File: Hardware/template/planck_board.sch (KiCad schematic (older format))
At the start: 3 parts, among them J1 Conn_01x40

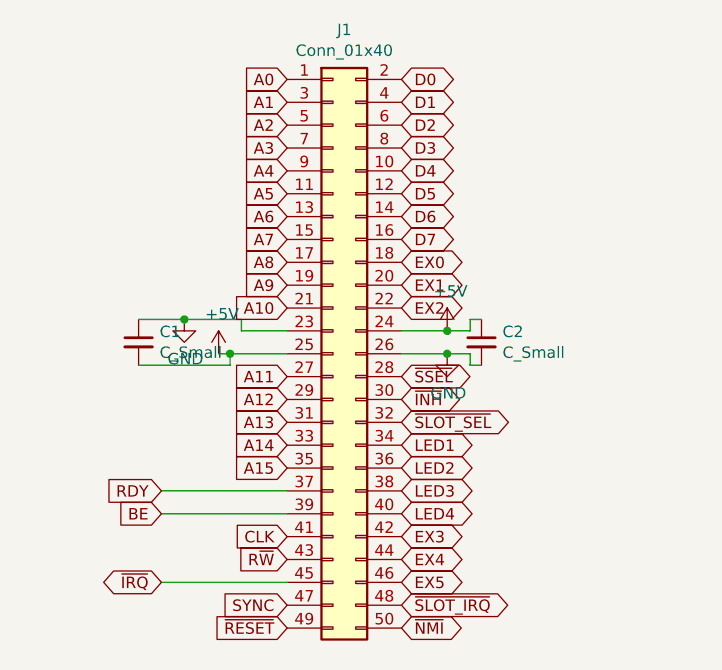
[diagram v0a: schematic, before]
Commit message: Space pins for better legibility
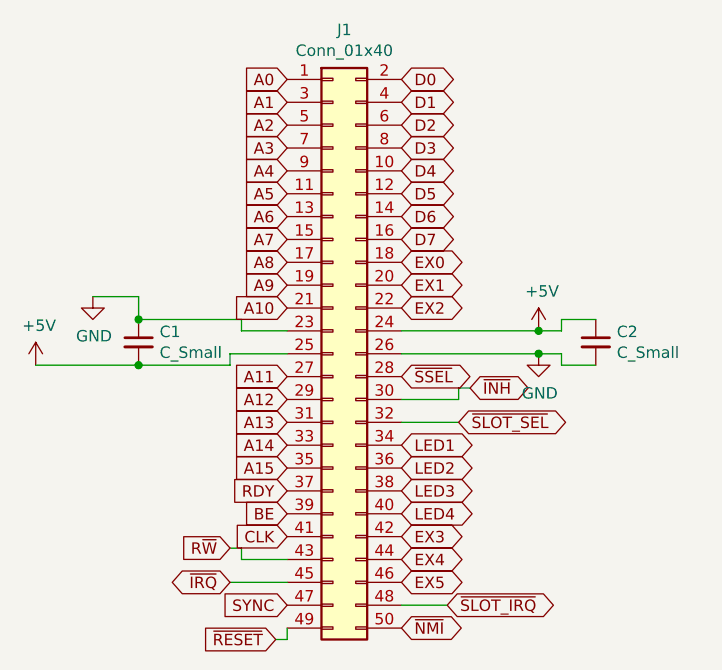
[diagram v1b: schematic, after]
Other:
- moved on the sheet: C2
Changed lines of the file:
@@
 L power:+5V #PWR0101
 U 1 1 5FD64472
-P 2650 3450
-F 0 "#PWR0101" H 2650 3300 50  0001 C CNN
-F 1 "+5V" H 2665 3623 50  0000 C CNN
-F 2 "" H 2650 3450 50  0001 C CNN
-F 3 "" H 2650 3450 50  0001 C CNN
-	1    2650 3450
-	1    0    0    -1
-$EndComp
-Wire Wire Line
-	2650 3450 2450 3450
+P 3050 3450
+F 0 "#PWR0101" H 3050 3300 50  0001 C CNN
+F 1 "+5V" H 3065 3623 50  0000 C CNN
+F 2 "" H 3050 3450 50  0001 C CNN
+F 3 "" H 3050 3450 50  0001 C CNN
+	1    3050 3450
+	1    0    0    -1
+$EndComp
 $Comp
 L power:+5V #PWR0102
 U 1 1 5FD65A34
-P 1650 3550
-F 0 "#PWR0102" H 1650 3400 50  0001 C CNN
-F 1 "+5V" H 1665 3723 50  0000 C CNN
-F 2 "" H 1650 3550 50  0001 C CNN
-F 3 "" H 1650 3550 50  0001 C CNN
-	1    1650 3550
+P 850 3600
+F 0 "#PWR0102" H 850 3450 50  0001 C CNN
+F 1 "+5V" H 865 3773 50  0000 C CNN
+F 2 "" H 850 3600 50  0001 C CNN
+F 3 "" H 850 3600 50  0001 C CNN
+	1    850  3600
 	1    0    0    -1
 $EndComp
@@
 L power:GND #PWR0103
 U 1 1 5FD65E00
-P 2650 3550
-F 0 "#PWR0103" H 2650 3300 50  0001 C CNN
-F 1 "GND" H 2655 3377 50  0000 C CNN
-F 2 "" H 2650 3550 50  0001 C CNN
-F 3 "" H 2650 3550 50  0001 C CNN
-	1    2650 3550
-	1    0    0    -1
-$EndComp
-Wire Wire Line
-	2650 3550 2450 3550
+P 3050 3550
+F 0 "#PWR0103" H 3050 3300 50  0001 C CNN
+F 1 "GND" H 3055 3377 50  0000 C CNN
+F 2 "" H 3050 3550 50  0001 C CNN
+F 3 "" H 3050 3550 50  0001 C CNN
+	1    3050 3550
+	1    0    0    -1
+$EndComp
 $Comp
 L power:GND #PWR0104
 U 1 1 5FD66D1A
-P 1500 3400
-F 0 "#PWR0104" H 1500 3150 50  0001 C CNN
-F 1 "GND" H 1505 3227 50  0000 C CNN
-F 2 "" H 1500 3400 50  0001 C CNN
-F 3 "" H 1500 3400 50  0001 C CNN
-	1    1500 3400
+P 1100 3300
+F 0 "#PWR0104" H 1100 3050 50  0001 C CNN
+F 1 "GND" H 1105 3127 50  0000 C CNN
+F 2 "" H 1100 3300 50  0001 C CNN
+F 3 "" H 1100 3300 50  0001 C CNN
+	1    1100 3300
 	1    0    0    -1
 $EndComp
 Wire Wire Line
 	1750 3450 1750 3400
-Wire Wire Line
-	1750 3400 1500 3400
 Wire Wire Line
 	1750 3450 1950 3450
@@
 Text GLabel 2450 3050 2    50   BiDi ~ 0
 D7
-Text GLabel 1950 4750 0    50   Input ~ 0
+Text GLabel 1900 4800 0    50   Input ~ 0
 ~RESET~
 Text GLabel 2450 4750 2    50   BiDi ~ 0
 ~NMI~
-Text GLabel 1400 4150 0    50   Input ~ 0
+Text GLabel 1950 4150 0    50   Input ~ 0
 RDY
-Text GLabel 1400 4250 0    50   Input ~ 0
+Text GLabel 1950 4250 0    50   Input ~ 0
 BE
 Text GLabel 1950 4350 0    50   Input ~ 0
 CLK
-Text GLabel 1950 4450 0    50   Input ~ 0
+Text GLabel 1700 4400 0    50   Input ~ 0
 R~W~
 Text GLabel 1950 4650 0    50   Input ~ 0
 SYNC
-Text GLabel 1400 4550 0    50   BiDi ~ 0
+Text GLabel 1700 4550 0    50   BiDi ~ 0
 ~IRQ~
-Text GLabel 2450 4650 2    50   BiDi ~ 0
+Text GLabel 2650 4650 2    50   BiDi ~ 0
 ~SLOT_IRQ~
 Text GLabel 2450 4550 2    50   BiDi ~ 0
@@
 L Device:C_Small C2
 U 1 1 5FD8A65F
-P 2800 3500
-F 0 "C2" H 2892 3546 50  0000 L CNN
-F 1 "C_Small" H 2892 3455 50  0000 L CNN
-F 2 "Capacitor_SMD:C_1206_3216Metric_Pad1.42x1.75mm_HandSolder" H 2800 3500 50  0001 C CNN
-F 3 "~" H 2800 3500 50  0001 C CNN
-	1    2800 3500
-	1    0    0    -1
-$EndComp
-Wire Wire Line
-	2800 3400 2750 3400
-Wire Wire Line
-	2750 3400 2750 3450
-Wire Wire Line
-	2750 3450 2650 3450
-Connection ~ 2650 3450
-Wire Wire Line
-	2800 3600 2750 3600
-Wire Wire Line
-	2750 3600 2750 3550
-Wire Wire Line
-	2750 3550 2650 3550
-Connection ~ 2650 3550
+P 3300 3500
+F 0 "C2" H 3392 3546 50  0000 L CNN
+F 1 "C_Small" H 3392 3455 50  0000 L CNN
+F 2 "Capacitor_SMD:C_1206_3216Metric_Pad1.42x1.75mm_HandSolder" H 3300 3500 50  0001 C CNN
+F 3 "~" H 3300 3500 50  0001 C CNN
+	1    3300 3500
+	1    0    0    -1
+$EndComp
+Wire Wire Line
+	3150 3400 3150 3450
+Wire Wire Line
+	3150 3600 3150 3550
+Wire Wire Line
+	3150 3550 3050 3550
 $Comp
 L Device:C_Small C1
@@
 $EndComp
 Wire Wire Line
-	1300 3400 1500 3400
-Connection ~ 1500 3400
-Wire Wire Line
 	1300 3600 1700 3600
 Wire Wire Line
 	1700 3600 1700 3550
-Connection ~ 1700 3550
-Wire Wire Line
-	1700 3550 1650 3550
-Wire Wire Line
-	1400 4550 1950 4550
-Wire Wire Line
-	1400 4150 1950 4150
-Wire Wire Line
-	1400 4250 1950 4250
+Wire Wire Line
+	1700 4550 1950 4550
 Text GLabel 2450 3650 2    50   BiDi ~ 0
 ~SSEL~
-Text GLabel 2450 3750 2    50   BiDi ~ 0
+Text GLabel 2750 3700 2    50   BiDi ~ 0
 ~INH~
-Text GLabel 2450 3850 2    50   BiDi ~ 0
+Text GLabel 2700 3850 2    50   BiDi ~ 0
 ~SLOT_SEL~
 Text GLabel 2450 3950 2    50   BiDi ~ 0
@@
 Text GLabel 2450 3350 2    50   BiDi ~ 0
 EX2
+Wire Wire Line
+	2450 3450 3050 3450
+Connection ~ 3050 3450
+Wire Wire Line
+	3050 3450 3150 3450
+Wire Wire Line
+	3150 3400 3300 3400
+Wire Wire Line
+	2450 3550 3050 3550
+Connection ~ 3050 3550
+Wire Wire Line
+	3150 3600 3300 3600
+Wire Wire Line
+	2750 3700 2700 3700
+Wire Wire Line
+	2700 3700 2700 3750
+Wire Wire Line
+	2700 3750 2450 3750
+Wire Wire Line
+	2650 4650 2450 4650
+Wire Wire Line
+	1900 4800 1950 4800
+Wire Wire Line
+	1950 4800 1950 4750
+Wire Wire Line
+	1700 4400 1750 4400
+Wire Wire Line
+	1750 4400 1750 4450
+Wire Wire Line
+	1750 4450 1950 4450
+Wire Wire Line
+	2700 3850 2450 3850
+Wire Wire Line
+	1300 3400 1750 3400
+Wire Wire Line
+	1300 3400 1300 3300
+Wire Wire Line
+	1300 3300 1100 3300
+Connection ~ 1300 3400
+Wire Wire Line
+	1300 3600 850  3600
+Connection ~ 1300 3600
 $EndSCHEMATC

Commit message: Add clock stretching with counter and slow clock request from peripherals.
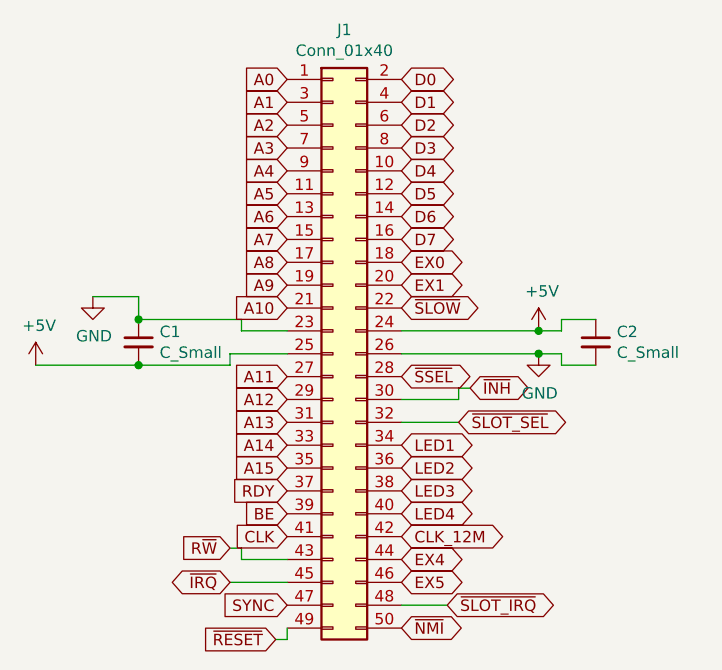
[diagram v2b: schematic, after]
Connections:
- net EX2 renamed ~SLOW~
- net EX3 renamed CLK_12M
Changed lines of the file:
@@
 EX4
 Text GLabel 2450 4350 2    50   BiDi ~ 0
-EX3
+CLK_12M
 $Comp
 L Device:C_Small C2
@@
 EX1
 Text GLabel 2450 3350 2    50   BiDi ~ 0
-EX2
+~SLOW~
 Wire Wire Line
 	2450 3450 3050 3450

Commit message: Many updates. SLOW signal is now shared amongst all slots, so their output has to be open drain.
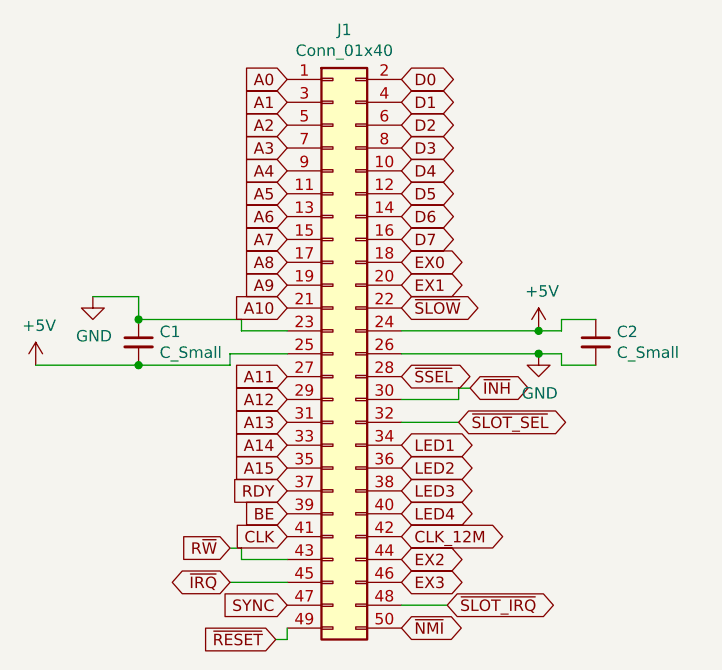
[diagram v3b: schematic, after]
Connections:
- net EX4 renamed EX2
- net EX5 renamed EX3
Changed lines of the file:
@@
 ~SLOT_IRQ~
 Text GLabel 2450 4550 2    50   BiDi ~ 0
-EX5
+EX3
 Text GLabel 2450 4450 2    50   BiDi ~ 0
-EX4
+EX2
 Text GLabel 2450 4350 2    50   BiDi ~ 0
 CLK_12M

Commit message: update pin names
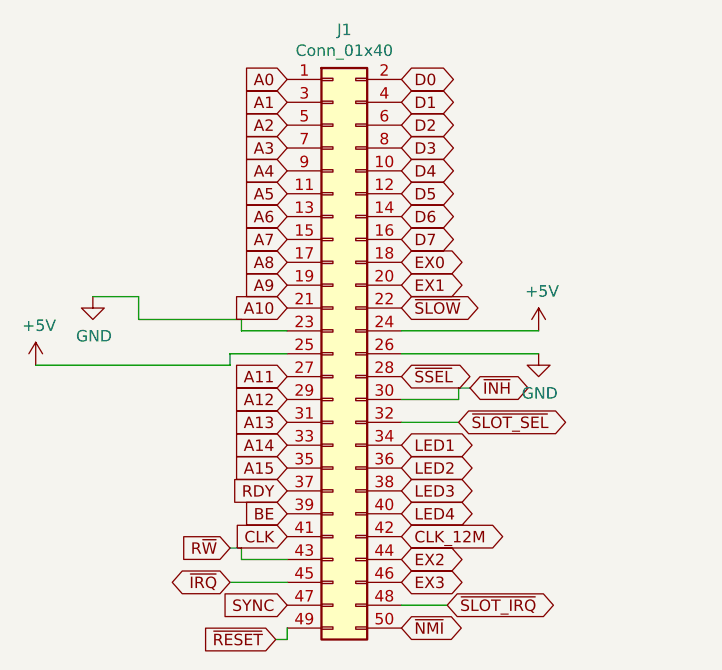
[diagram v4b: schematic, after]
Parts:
- removed C1, C2: C_Small, Capacitor_SMD:C_1206_3216Metric_Pad1.42x1.75mm_HandSolder, symbol Device:C_Small
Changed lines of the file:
@@
 Text GLabel 2450 4350 2    50   BiDi ~ 0
 CLK_12M
-$Comp
-L Device:C_Small C2
-U 1 1 5FD8A65F
-P 3300 3500
-F 0 "C2" H 3392 3546 50  0000 L CNN
-F 1 "C_Small" H 3392 3455 50  0000 L CNN
-F 2 "Capacitor_SMD:C_1206_3216Metric_Pad1.42x1.75mm_HandSolder" H 3300 3500 50  0001 C CNN
-F 3 "~" H 3300 3500 50  0001 C CNN
-	1    3300 3500
-	1    0    0    -1
-$EndComp
-Wire Wire Line
-	3150 3400 3150 3450
-Wire Wire Line
-	3150 3600 3150 3550
-Wire Wire Line
-	3150 3550 3050 3550
-$Comp
-L Device:C_Small C1
-U 1 1 5FD8C99F
-P 1300 3500
-F 0 "C1" H 1392 3546 50  0000 L CNN
-F 1 "C_Small" H 1392 3455 50  0000 L CNN
-F 2 "Capacitor_SMD:C_1206_3216Metric_Pad1.42x1.75mm_HandSolder" H 1300 3500 50  0001 C CNN
-F 3 "~" H 1300 3500 50  0001 C CNN
-	1    1300 3500
-	1    0    0    -1
-$EndComp
-Wire Wire Line
-	1300 3600 1700 3600
 Wire Wire Line
 	1700 3600 1700 3550
@@
 Wire Wire Line
 	2450 3450 3050 3450
-Connection ~ 3050 3450
-Wire Wire Line
-	3050 3450 3150 3450
-Wire Wire Line
-	3150 3400 3300 3400
 Wire Wire Line
 	2450 3550 3050 3550
-Connection ~ 3050 3550
-Wire Wire Line
-	3150 3600 3300 3600
 Wire Wire Line
 	2750 3700 2700 3700
@@
 Wire Wire Line
 	1300 3300 1100 3300
-Connection ~ 1300 3400
 Wire Wire Line
-	1300 3600 850  3600
-Connection ~ 1300 3600
+	850  3600 1700 3600
 $EndSCHEMATC
